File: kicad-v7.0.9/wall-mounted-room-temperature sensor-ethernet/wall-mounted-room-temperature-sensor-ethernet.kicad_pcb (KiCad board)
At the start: 2 copper layers, 107 x 90 mm, 165 parts, among them J1 54601-908WPLF, P1 2x3_MLW06A, P2 DS1023-1-9S21, Q1 DMG2307L, Q2 FDC2512, SW1 TVAF18BB, SW2 TVAF18BB, SW3 B3F-4150, SW4 B3F-4150, SW5 B3F-4150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

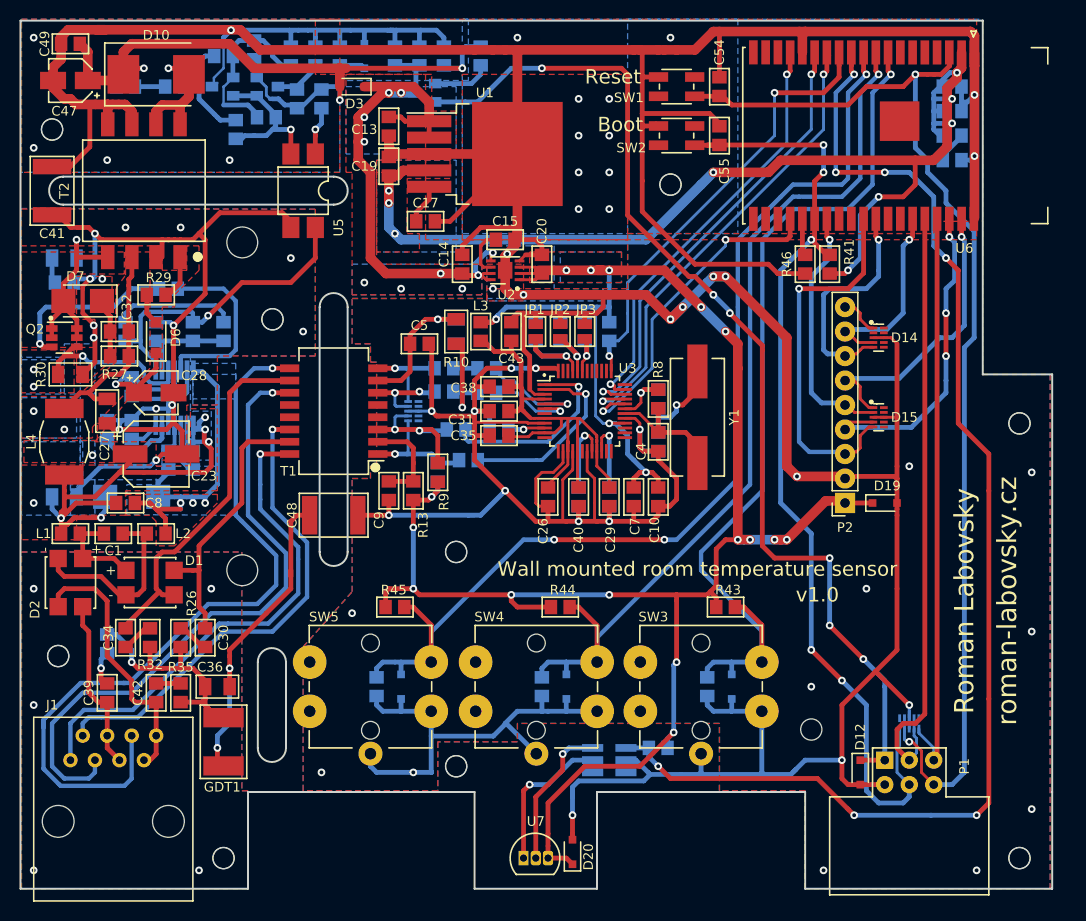
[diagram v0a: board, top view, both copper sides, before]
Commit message: Change components form library. Adding of BOM.
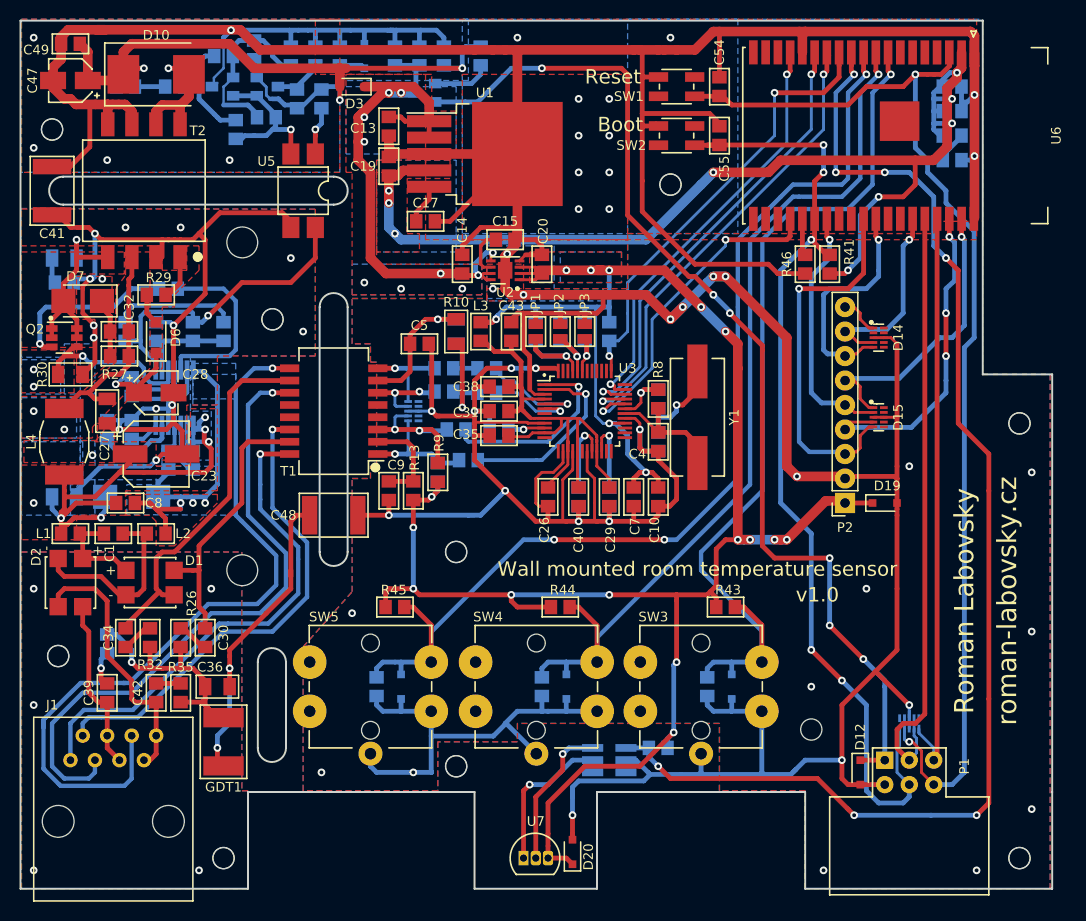
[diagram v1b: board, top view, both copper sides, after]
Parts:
- P1: footprint connector_idc_rl:2x3_MLW06A -> connector_idc_tht_rl:2x3_MLW06A
- P2: footprint connector_tht_pinsocket_2.54mm_rl:1x9_pinsocket_2.54mm_vertical_8.5mm -> connector_pin_socket_2.54mm_tht_rl:1x9_pin_socket_2.54mm_vertical_8.5mm
